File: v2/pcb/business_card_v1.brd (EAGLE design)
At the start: 89 x 51 mm, 71 parts, among them SW1 SPST_TACT-KMR2

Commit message: update pcb and schematic
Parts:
- removed ISP1: AVRISP-6, adafruit:AVRISP
- removed U$1: (no value), adafruit:OSHWLOGO_TOP_0.2
- IC1: device atmel_tiny24-44-84tiny48-88mega48-88-168-328:MLF20 -> atmel_tiny24-44-84tiny48-88mega48-88-168-328:SOIC14
- moved R9 349.0 mm to (85.1, 44.5), turned to 90 degrees
- moved LED56 347.0 mm to (85.1, 48.3), turned to 90 degrees
- moved R8 343.2 mm to (80.0, 44.5), turned to 90 degrees
- moved LED55 335.1 mm to (80.0, 48.3), turned to 90 degrees
- moved LED54 323.2 mm to (74.9, 48.3), turned to 90 degrees
- moved LED53 311.3 mm to (69.8, 48.3), turned to 90 degrees
- moved LED52 299.4 mm to (64.8, 48.3), turned to 90 degrees
- moved LED48 292.8 mm to (85.1, 53.3), turned to 90 degrees
- moved LED51 287.5 mm to (59.7, 48.3), turned to 90 degrees
- moved LED47 280.9 mm to (80.0, 53.3), turned to 90 degrees
- moved LED50 275.6 mm to (54.6, 48.3), turned to 90 degrees
- moved LED46 269.1 mm to (74.9, 53.3), turned to 90 degrees
- moved LED49 263.8 mm to (49.5, 48.3), turned to 90 degrees
- moved LED45 257.3 mm to (69.8, 53.3), turned to 90 degrees
- moved LED44 245.6 mm to (64.8, 53.3), turned to 90 degrees
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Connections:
- removed net +5V: C1.1, ISP1.2, JP1.5V, R1.2
- removed net N$12: LED13.A, LED14.C, LED15.C, LED18.A, LED23.A, LED28.C, LED3.A, LED33.C, LED38.A, LED47.A, LED54.C, LED8.A, R4.2
- removed net N$13: LED10.C, LED12.A, LED17.A, LED2.A, LED22.A, LED29.C, LED32.C, LED37.A, LED48.A, LED55.C, LED7.A, LED8.C, LED9.C, R3.2
- removed net N$5: LED1.C, LED13.C, LED19.C, LED25.C, LED41.C, LED43.C, LED50.A, LED51.A, LED52.A, LED53.A, LED54.A, LED55.A, LED56.A, LED7.C, R9.2
- removed net N$6: LED10.A, LED15.A, LED20.A, LED25.A, LED26.C, LED35.C, LED40.A, LED45.A, LED5.A, LED52.C, R6.2
- removed net N$9: LED14.A, LED19.A, LED20.C, LED24.A, LED27.C, LED34.C, LED39.A, LED4.A, LED46.A, LED53.C, LED9.A, R5.2
- new net N$15: LED10.C, LED11.C, LED12.C, LED13.C, LED14.C, LED15.A, LED23.A, LED31.A, LED39.A, LED47.A, LED55.A, LED7.A, LED8.C, LED9.C, R8.2
- new net N$31: LED14.A, LED15.C, LED16.C, LED17.C, LED18.C, LED19.C, LED20.C, LED21.C, LED22.A, LED30.A, LED38.A, LED46.A, LED54.A, LED6.A, R7.2
- new net N$34: LED13.A, LED21.A, LED22.C, LED23.C, LED24.C, LED25.C, LED26.C, LED27.C, LED28.C, LED29.A, LED37.A, LED45.A, LED5.A, LED53.A, R6.2
- new net N$8: LED1.C, LED16.A, LED2.C, LED24.A, LED3.C, LED32.A, LED4.C, LED40.A, LED48.A, LED5.C, LED56.A, LED6.C, LED7.C, LED8.A, R9.2
- new net PIN6: IC1.7, R8.1
- new net PIN7: IC1.6, R9.1
- net GND: now also IC1.14; no longer IC1.8, IC1.TH, ISP1.6
- net N$1: now also LED17.A, LED25.A, LED33.A, LED41.A, LED50.C, LED51.C, LED52.C, LED53.C, LED54.C, LED55.C, LED9.A; no longer LED11.A, LED16.A, LED2.C, LED21.A, LED3.C, LED30.C, LED31.C, LED36.A, LED4.C, LED5.C, LED6.A
- net N$2: now also LED10.A, LED18.A, LED2.A, LED34.A, LED42.A, LED43.C, LED44.C, LED45.C, LED46.C, LED47.C, LED48.C, LED49.C, LED50.A, R3.2; no longer LED27.A, LED28.A, LED29.A, LED30.A, LED41.A, LED42.C, LED44.A, LED51.C, R7.2
- net N$3: now also LED11.A, LED19.A, LED27.A, LED3.A, LED35.A, LED36.C, LED37.C, LED38.C, LED39.C, LED40.C, LED41.C, LED42.C, LED43.A, LED51.A, R4.2; no longer LED6.C
- net N$4: now also LED12.A, LED20.A, LED28.A, LED29.C, LED30.C, LED31.C, LED32.C, LED33.C, LED34.C, LED35.C, LED36.A, LED4.A, LED44.A, LED52.A, R5.2; no longer LED31.A, LED32.A, LED33.A, LED34.A, LED35.A, LED42.A, LED43.A, LED50.C, R8.2
- net PIN0: now also IC1.13, R2.1; no longer ISP1.4, R4.1
- net PIN1: now also IC1.12, R3.1; no longer ISP1.1, R2.1
- net PIN2: now also IC1.11, R4.1; no longer ISP1.3, R3.1
- net PIN3: now also IC1.10, R5.1; no longer R6.1
- net PIN4: now also IC1.9, R6.1; no longer R5.1
- net PIN5: now also IC1.8
- net RESET: now also IC1.4; no longer ISP1.5
- net UCC: now also C1.1, IC1.1, JP1.5V, R1.2; no longer IC1.9
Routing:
- removed copper zone on layer 1, net +5V
- removed copper zone on layer 16, net GND
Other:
- board size 89 x 51 mm -> 89 x 51.8 mm
- board text removed: "Electrical Engineering and Computer Science Major"
- board text removed: "Kevin Lutzer"
- board text removed: "kml183@mail.usask.ca"
- board text removed: "rev 1.0"
- board text removed: "www.kevinlutzer.ca"

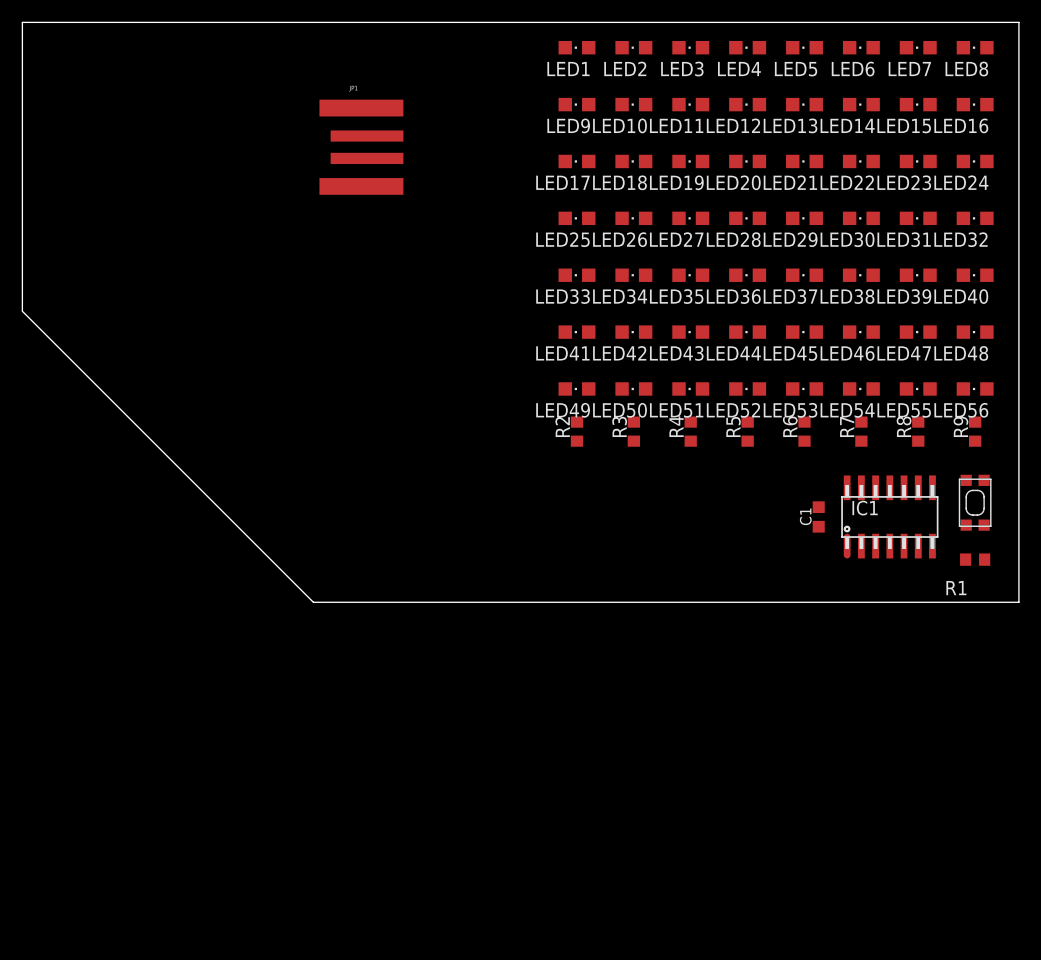
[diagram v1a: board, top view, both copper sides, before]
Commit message: route the led grid, add the silk screen
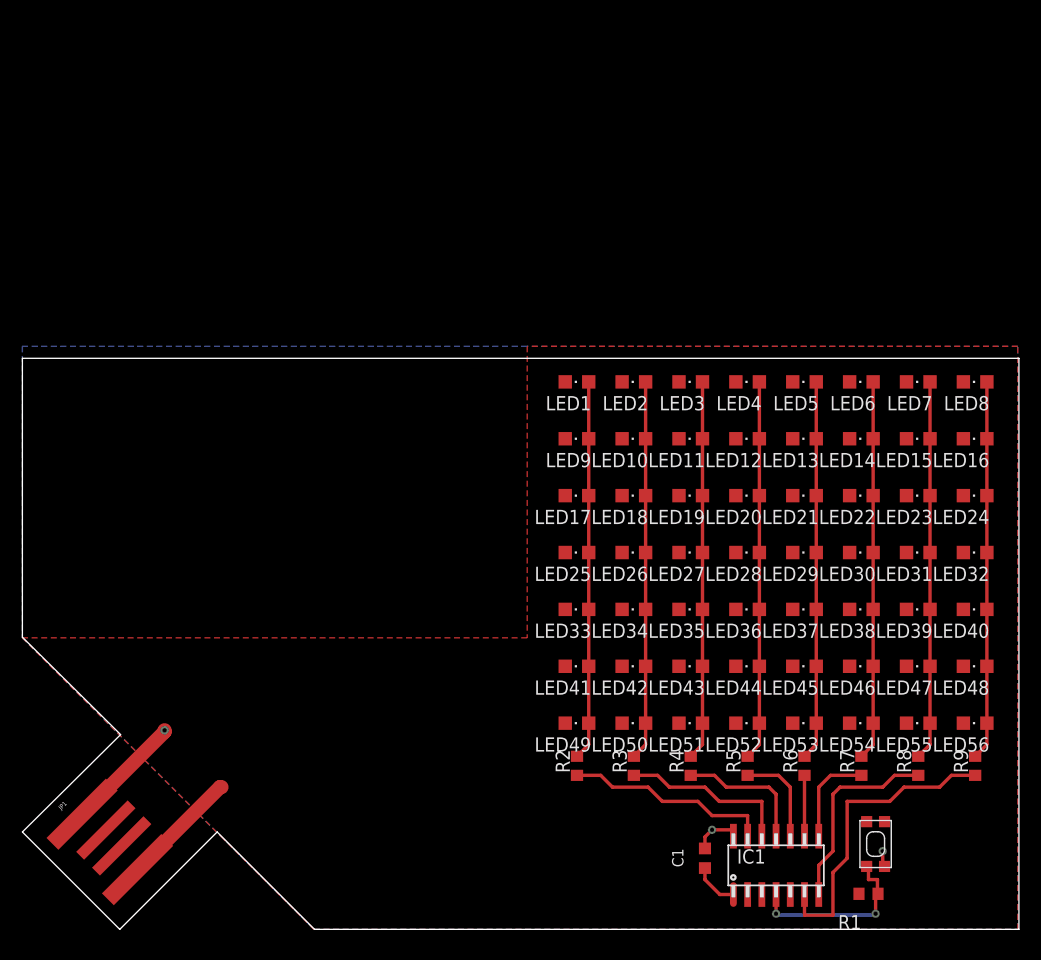
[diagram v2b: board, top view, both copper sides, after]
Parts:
- moved JP1 65.9 mm to (7.95, 7.95), turned to 45 degrees
- moved IC1 32.7 mm to (67.3, 5.71)
- moved C1 32.1 mm to (61.0, 6.35)
- moved SW1 31.8 mm to (76.2, 7.62)
- moved R1 31.3 mm to (75.6, 3.17)
- moved LED33 29.8 mm to (49.5, 28.6)
- moved LED34 29.8 mm to (54.6, 28.6)
- moved LED35 29.8 mm to (59.7, 28.6)
- moved LED36 29.8 mm to (64.8, 28.6)
- moved LED37 29.8 mm to (69.8, 28.6)
- moved LED38 29.8 mm to (74.9, 28.6)
- moved LED39 29.8 mm to (80.0, 28.6)
- moved LED40 29.8 mm to (85.1, 28.6)
- moved LED41 29.8 mm to (49.5, 23.5)
- moved LED42 29.8 mm to (54.6, 23.5)
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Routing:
- net N$34: track 0.00 -> 33.9 mm
- net N$3: track 0.00 -> 33.9 mm
- net N$8: track 0.00 -> 33.9 mm
- net N$4: track 0.00 -> 33.9 mm
- net N$31: track 0.00 -> 33.9 mm
- net N$2: track 0.00 -> 33.9 mm
- net N$15: track 0.00 -> 33.9 mm
- net N$1: track 0.00 -> 33.9 mm
- net PIN7: track 0.00 -> 27.5 mm
- net PIN0: track 0.00 -> 18.6 mm
- net PIN6: track 0.00 -> 17.8 mm
- net GND: track 0.00 -> 16.5 mm, vias 0 -> 3
- net RESET: track 0.00 -> 16.4 mm, vias 0 -> 2
- net PIN1: track 0.00 -> 15.5 mm
- net UCC: track 0.00 -> 14.9 mm
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- added copper zone on layer 16, net GND
- added copper zone on layer 1, net UCC
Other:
- board size 89 x 51.8 mm -> 89 x 51 mm

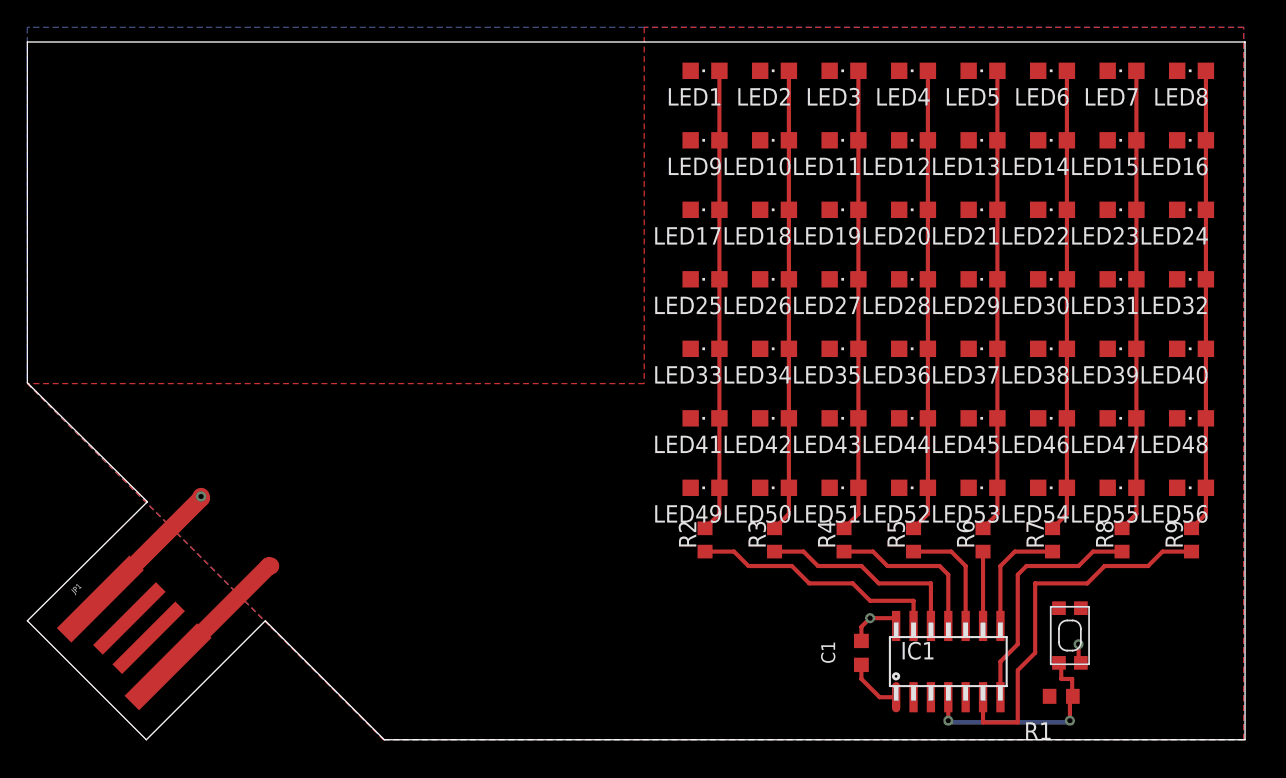
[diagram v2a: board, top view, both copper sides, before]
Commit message: finish of the routing and get personal information on silk screen
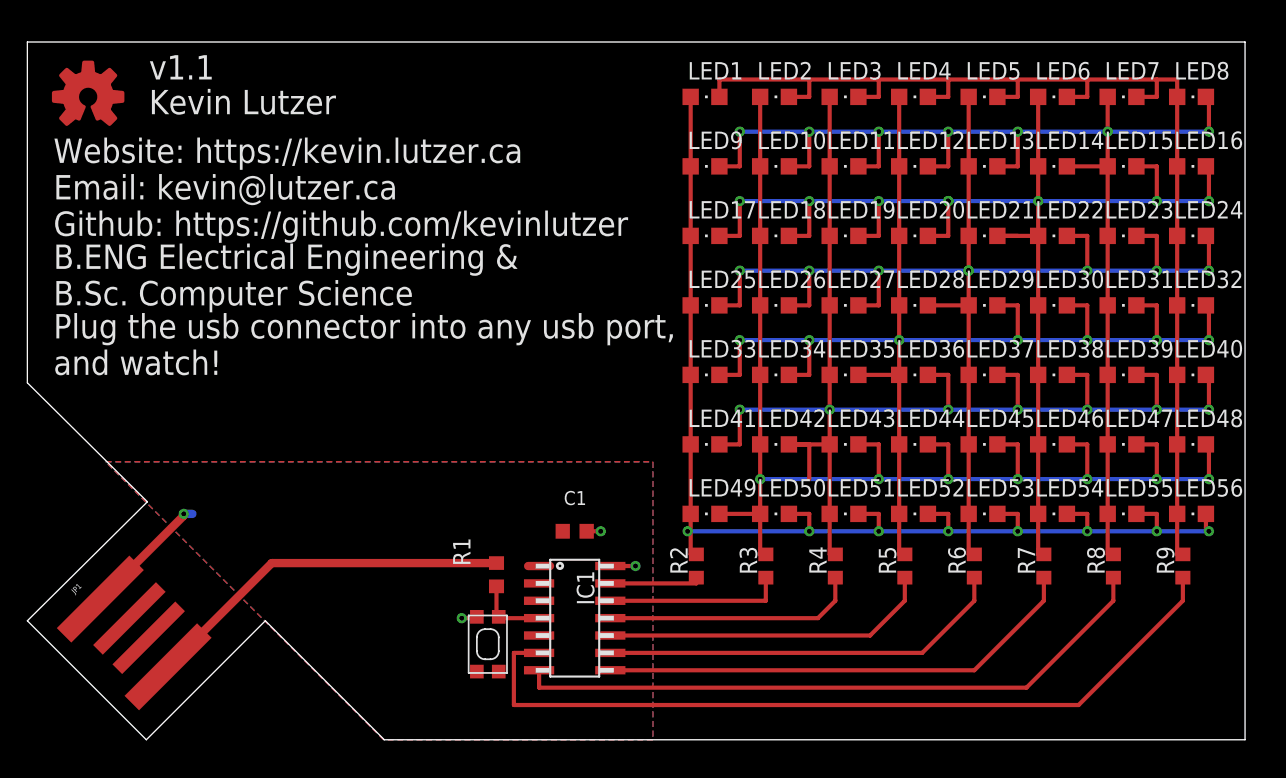
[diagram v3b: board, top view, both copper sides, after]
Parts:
- added U$1: (no value), adafruit:OSHWLOGO_TOP_0.2
- moved SW1 42.5 mm to (33.7, 6.99), turned to 270 degrees
- moved R1 42.2 mm to (34.3, 12.1), turned to 90 degrees
- moved IC1 27.5 mm to (40.0, 8.89), turned to 270 degrees
- moved C1 22.8 mm to (40.0, 15.2), turned to 0 degrees
- moved R7 2.01 mm to (74.3, 12.7)
- moved R8 2.01 mm to (79.4, 12.7)
- moved R9 2.01 mm to (84.5, 12.7)
- moved R2 2.01 mm to (48.9, 12.7)
- moved R3 2.01 mm to (54.0, 12.7)
- moved R4 2.01 mm to (59.1, 12.7)
- moved R5 2.01 mm to (64.1, 12.7)
- moved R6 2.01 mm to (69.2, 12.7)
- moved LED1 1.91 mm to (49.5, 47.0), turned to 270 degrees
- moved LED10 1.91 mm to (54.6, 41.9), turned to 270 degrees
- moved LED11 1.91 mm to (59.7, 41.9), turned to 270 degrees
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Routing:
- net N$3: track 33.9 -> 98.1 mm, vias 0 -> 7
- net N$31: track 33.9 -> 95.5 mm, vias 0 -> 8
- net N$15: track 33.9 -> 94.0 mm, vias 0 -> 7
- net N$34: track 33.9 -> 94.0 mm, vias 0 -> 8
- net N$4: track 33.9 -> 94.0 mm, vias 0 -> 7
- net N$2: track 33.9 -> 92.5 mm, vias 0 -> 7
- net N$1: track 33.9 -> 90.1 mm, vias 0 -> 8
- net N$8: track 33.9 -> 86.4 mm
- net PIN7: track 27.5 -> 59.4 mm
- net PIN6: track 17.8 -> 47.6 mm
- net PIN5: track 8.63 -> 35.5 mm
- net PIN4: track 5.44 -> 29.9 mm
- net PIN3: track 8.93 -> 24.3 mm
- net UCC: track 14.9 -> 27.3 mm
- net PIN0: track 18.6 -> 6.71 mm
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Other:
- board text added: "B.ENG Electrical Engineering & B.Sc. Computer Science"
- board text added: "Kevin Lutzer"
- board text added: "Plug the usb connector into any usb port, and watch!"
- board text added: "Website: https://kevin.lutzer.ca Email: kevin@lutzer.ca Github: https://github.com/kevinlutzer"
- board text added: "v1.1"

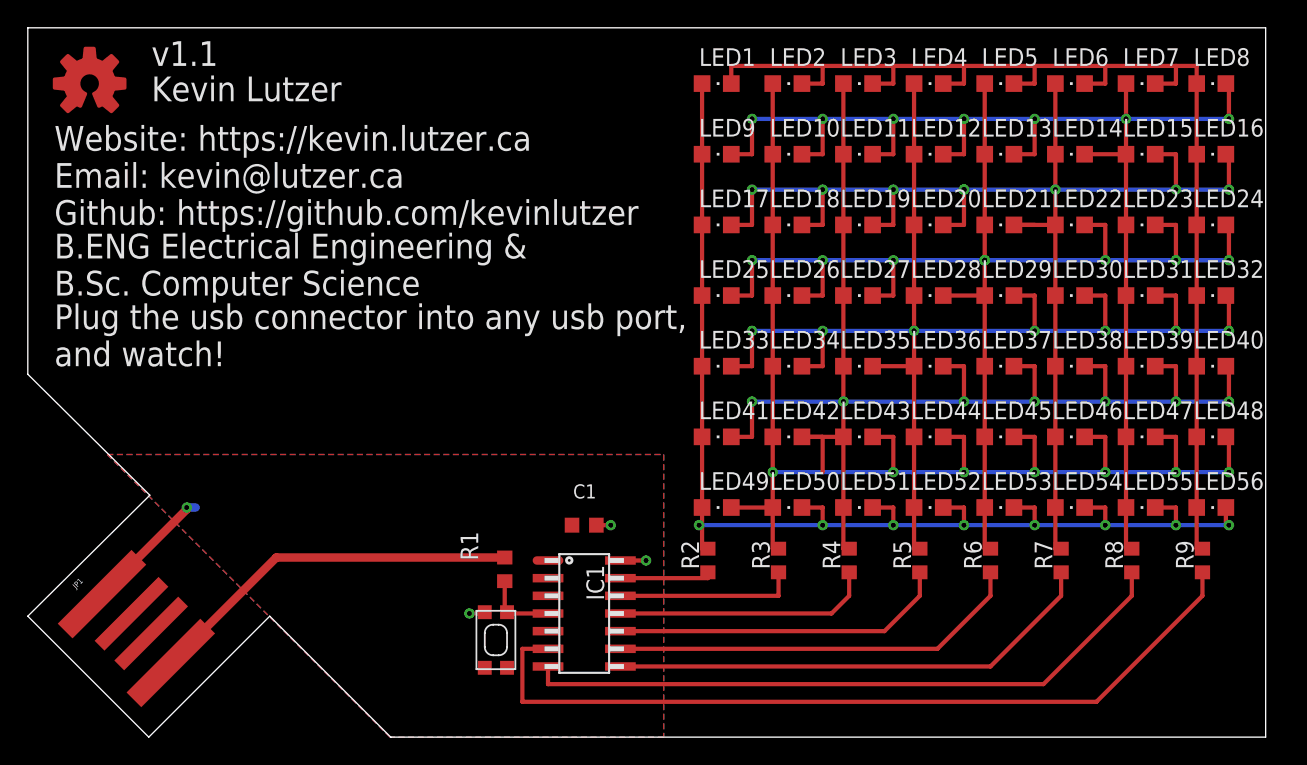
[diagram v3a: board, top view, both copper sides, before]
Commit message: fix the business card design
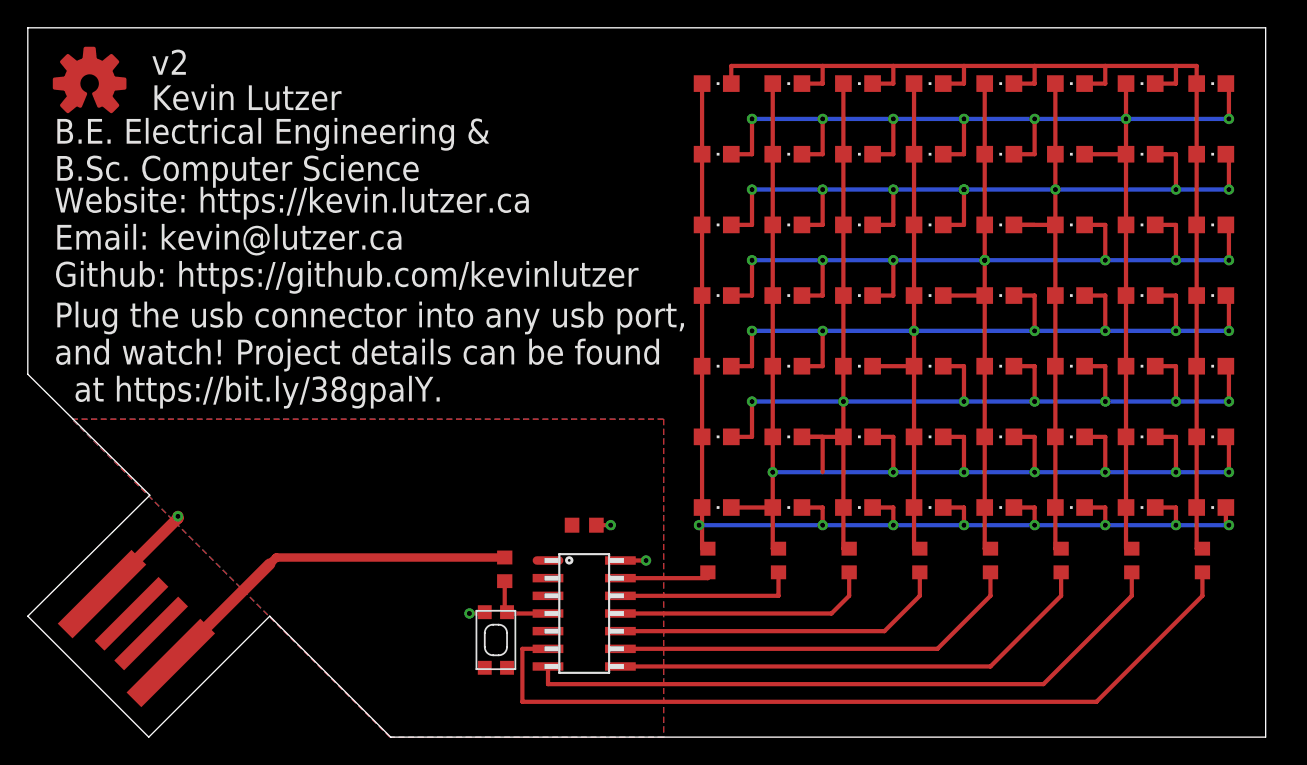
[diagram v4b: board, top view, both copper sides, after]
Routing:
- net GND: track 13.4 -> 12.0 mm
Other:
- board text added: "B.E. Electrical Engineering & B.Sc. Computer Science"
- board text added: "Plug the usb connector into any usb port, and watch! Project details can be found at https://bit.ly/38gpalY."
- board text added: "v2"
- board text removed: "B.ENG Electrical Engineering & B.Sc. Computer Science"
- board text removed: "Plug the usb connector into any usb port, and watch!"
- board text removed: "v1.1"
